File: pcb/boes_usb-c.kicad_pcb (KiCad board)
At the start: 2 copper layers, 38.1 x 26 mm, 9 parts, among them J1 USB_C_Receptacle_USB2.0

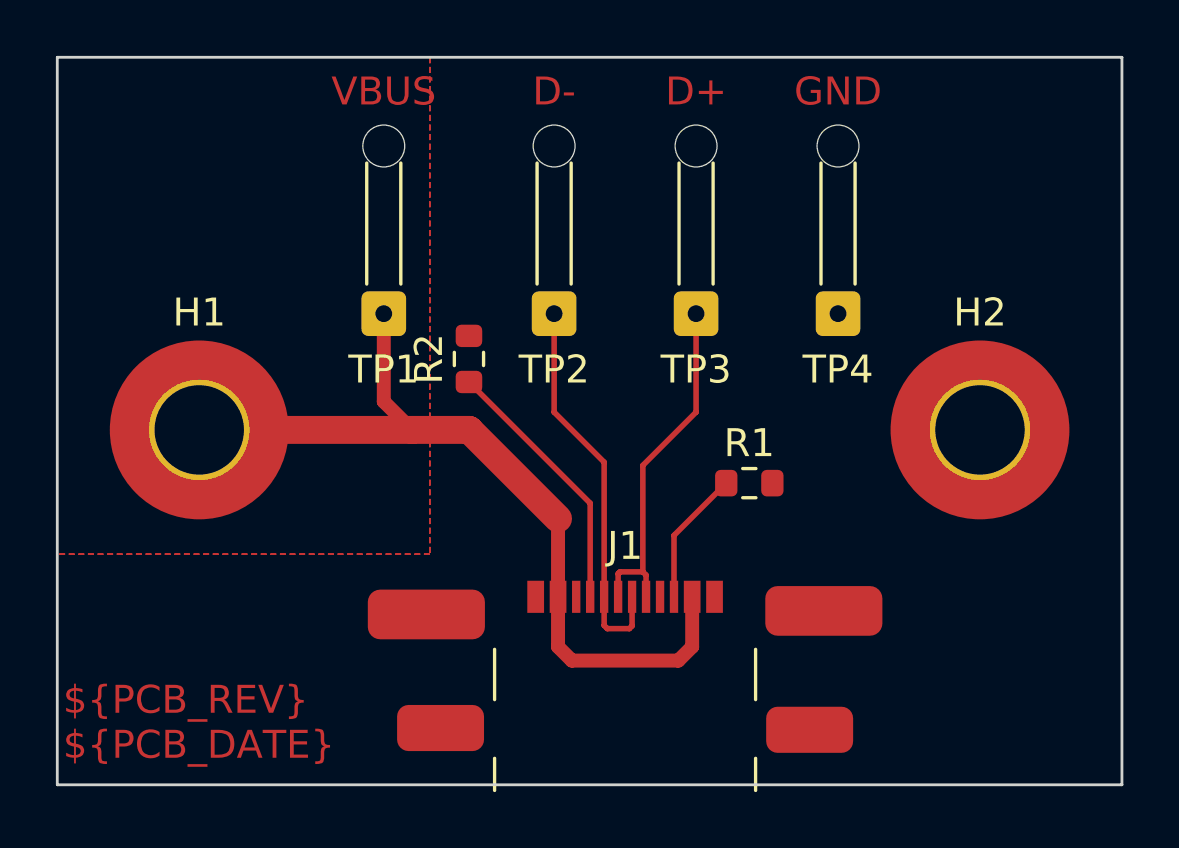
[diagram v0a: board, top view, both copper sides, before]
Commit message: Improve VBUS filled zone
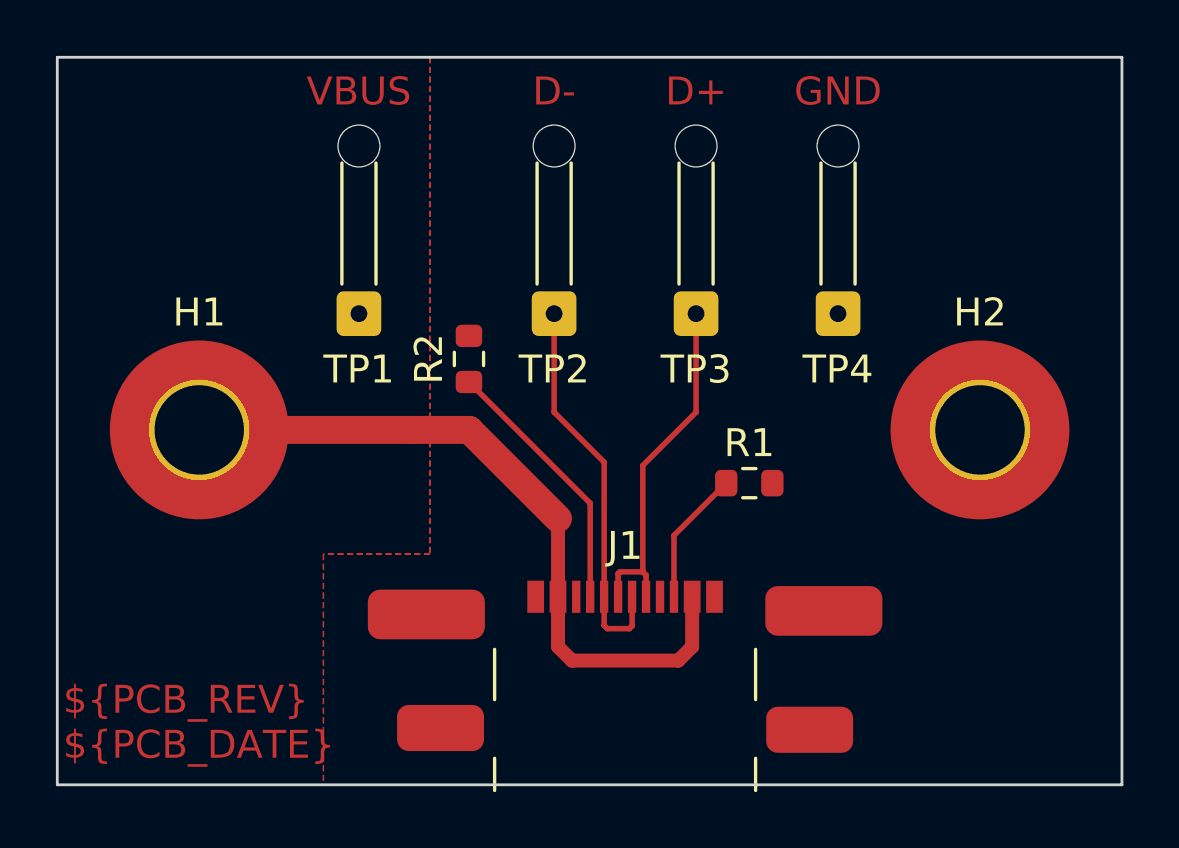
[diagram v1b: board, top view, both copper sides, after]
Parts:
- moved TP1 0.89 mm to (92.1, 59.3)
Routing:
- net VBUS: track 30.3 -> 25.7 mm

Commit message: Improve strain relief
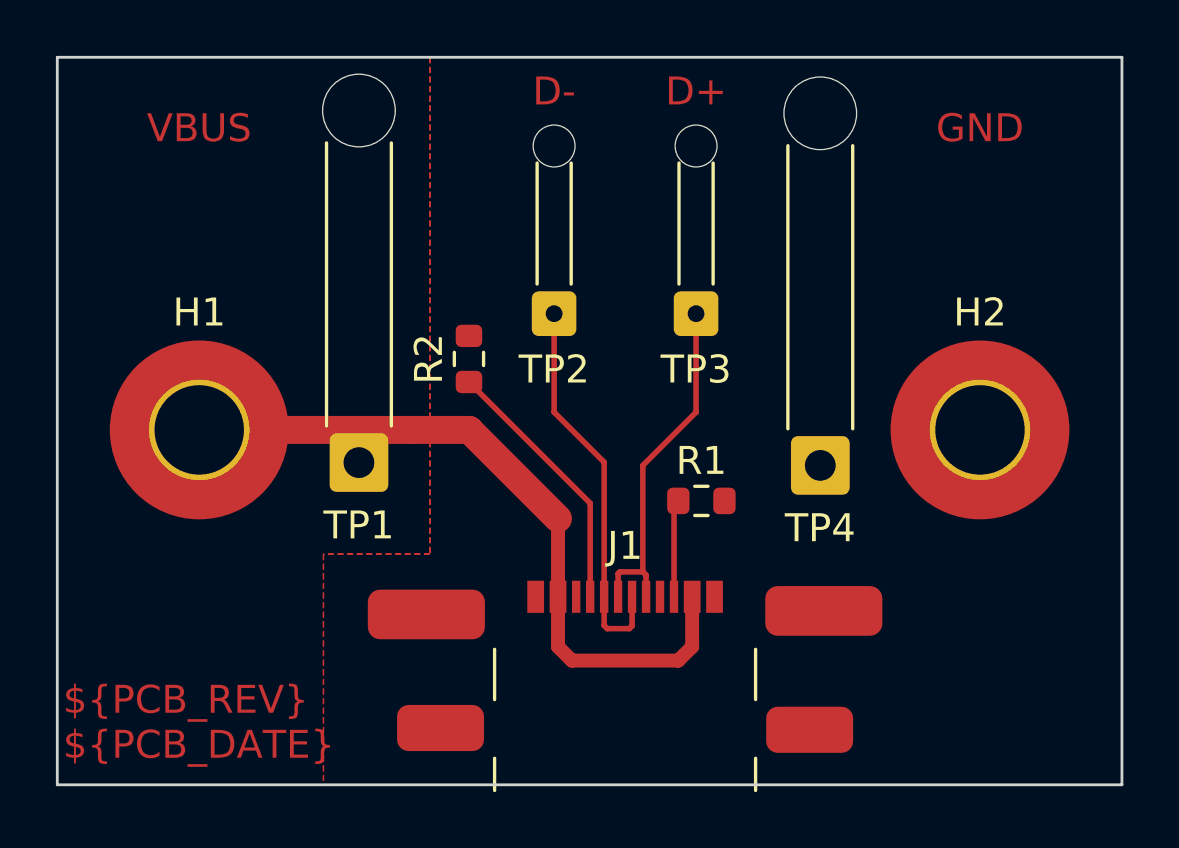
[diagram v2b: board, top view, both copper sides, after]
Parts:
- TP1, TP4: footprint Connector_Wire:SolderWire-0.1sqmm_1x01_D0.4mm_OD1mm_Relief -> Connector_Wire:SolderWire-0.5sqmm_1x01_D0.9mm_OD2.1mm_Relief
- moved TP4 5.47 mm to (108.6, 64.8)
- moved TP1 5.33 mm to (92.1, 64.7)
- moved R1 1.83 mm to (104.3, 66.0)
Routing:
- net Net-(J1-CC2): track 4.84 -> 3.50 mm
